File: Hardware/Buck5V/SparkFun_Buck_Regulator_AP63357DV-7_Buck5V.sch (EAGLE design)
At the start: 29 parts, among them J3 POWER_JACK, U1 AP63357

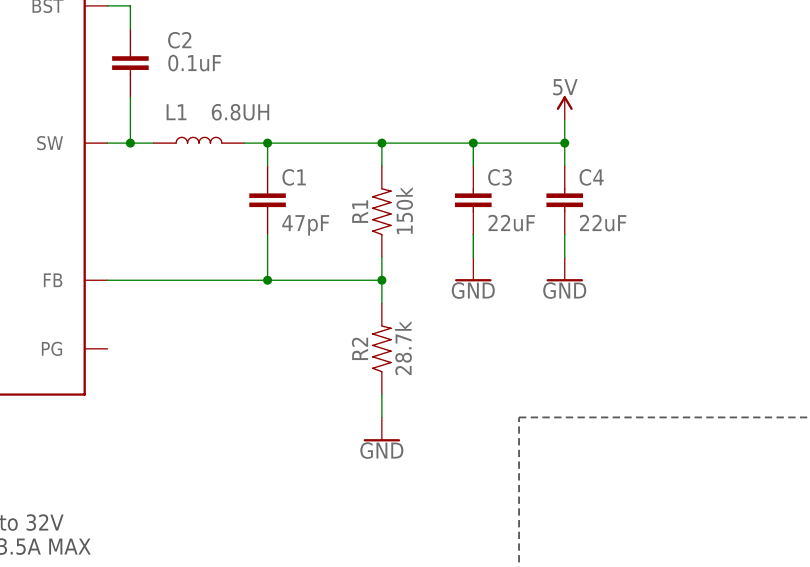
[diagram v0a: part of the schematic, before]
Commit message: Prepare for v10 reds order.
Change R1/R2 to better match 5V output requirement.
Repanelize.
Reorganize Production Folder Structure.
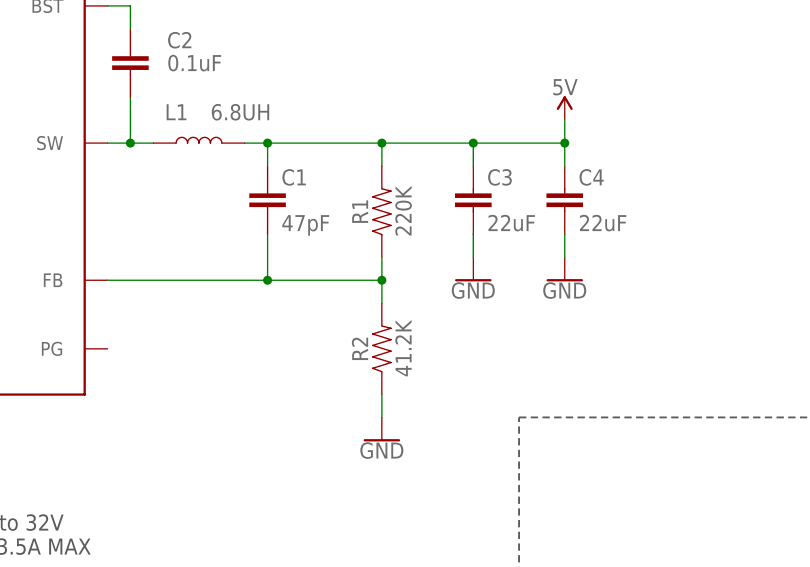
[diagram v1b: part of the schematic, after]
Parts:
- R1: value 150k -> 220K; device SparkFun-Resistors:150KOHM-0402T-1/16W-1% -> SparkFun-Resistors:220KOHM-0402T-1/16W-1%; RES 150k -> (none)
- R2: value 28.7k -> 41.2K; device Buck5V:28.7KOHM-0402-1/16W-1%(28.7KOHM) -> Buck5V:41.2KOHM-0402-1/16W-1%(41.2KOHM)
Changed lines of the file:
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@@
 <part name="J3" library="SparkFun-Connectors" deviceset="POWER_JACK" device="POWER_JACK_SLOT_NO_SILK_OVRHNG" value="POWER_JACK"/>
 <part name="J2" library="SparkFun-Connectors" deviceset="CONN_05" device="NO_SILK"/>
-<part name="R2" library="Buck5V" deviceset="28.7KOHM" device="-0402-1/16W-1%(28.7KOHM)" value="28.7k"/>
+<part name="R2" library="Buck5V" deviceset="41.2KOHM" device="-0402-1/16W-1%(41.2KOHM)" value="41.2K"/>
 <part name="U1" library="Buck5V" deviceset="AP63357" device="" value="AP63357"/>
-<part name="R1" library="SparkFun-Resistors" deviceset="150KOHM" device="-0402T-1/16W-1%" value="150k">
-<attribute name="RES" value="150k"/>
-</part>
 <part name="C1" library="SparkFun-Capacitors" deviceset="47PF" device="-0402_TIGHT-25V-5%-X7R" value="47pF"/>
 <part name="L1" library="Buck5V" deviceset="6.8UH" device="" value="6.8UH"/>
@@
 <part name="C6" library="SparkFun-Capacitors" deviceset="4.7UF" device="-0805-50V-(10%)" value="4.7uF"/>
 <part name="GND10" library="SparkFun-PowerSymbols" deviceset="GND" device=""/>
+<part name="R1" library="SparkFun-Resistors" deviceset="220KOHM" device="-0402T-1/16W-1%" value="220K"/>
 </parts>
 <sheets>
@@
 <attribute name="VALUE" x="48.26" y="66.04" size="1.778" layer="96" font="vector"/>
 </instance>
-<instance part="R1" gate="G$1" x="106.68" y="91.44" smashed="yes" rot="R90">
-<attribute name="NAME" x="105.156" y="91.44" size="1.778" layer="95" font="vector" rot="R90" align="bottom-center"/>
-<attribute name="RES" x="109.22" y="91.44" size="1.778" layer="96" font="vector" rot="R90" align="center"/>
-</instance>
 <instance part="C1" gate="G$1" x="93.98" y="91.44" smashed="yes">
 <attribute name="NAME" x="95.504" y="94.361" size="1.778" layer="95" font="vector"/>
@@
 <attribute name="VALUE" x="22.86" y="98.806" size="1.778" layer="96" font="vector" align="top-center"/>
 </instance>
+<instance part="R1" gate="G$1" x="106.68" y="91.44" smashed="yes" rot="R90">
+<attribute name="NAME" x="105.156" y="91.44" size="1.778" layer="95" font="vector" rot="R90" align="bottom-center"/>
+<attribute name="VALUE" x="108.204" y="91.44" size="1.778" layer="96" font="vector" rot="R90" align="top-center"/>
+</instance>
 </instances>
 <busses>
@@
 <segment>
 <pinref part="U1" gate="G$1" pin="FB"/>
-<pinref part="R1" gate="G$1" pin="1"/>
 <wire x1="76.2" y1="83.82" x2="93.98" y2="83.82" width="0.1524" layer="91"/>
 <wire x1="93.98" y1="83.82" x2="106.68" y2="83.82" width="0.1524" layer="91"/>
@@
 <wire x1="93.98" y1="88.9" x2="93.98" y2="83.82" width="0.1524" layer="91"/>
 <junction x="93.98" y="83.82"/>
+<pinref part="R1" gate="G$1" pin="1"/>
 </segment>
 </net>
@@
 <net name="5V" class="0">
 <segment>
-<pinref part="R1" gate="G$1" pin="2"/>
 <wire x1="106.68" y1="96.52" x2="106.68" y2="99.06" width="0.1524" layer="91"/>
 <wire x1="106.68" y1="99.06" x2="93.98" y2="99.06" width="0.1524" layer="91"/>
@@
 <wire x1="127" y1="99.06" x2="127" y2="101.6" width="0.1524" layer="91"/>
 <junction x="127" y="99.06"/>
-</segment>
-<segment>
+<pinref part="R1" gate="G$1" pin="2"/>
+</segment>
+<segment>
